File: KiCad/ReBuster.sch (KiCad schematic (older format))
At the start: 11 parts, among them U3 SN74CBTD16210, U4 SN74LVC16T245DGVR, U5 SN74CBTD16210, U6 SN74CBTD16210, U7 74LVC2T45DC, U8 PLCC_84_plug, U9 PLCC_84_plug

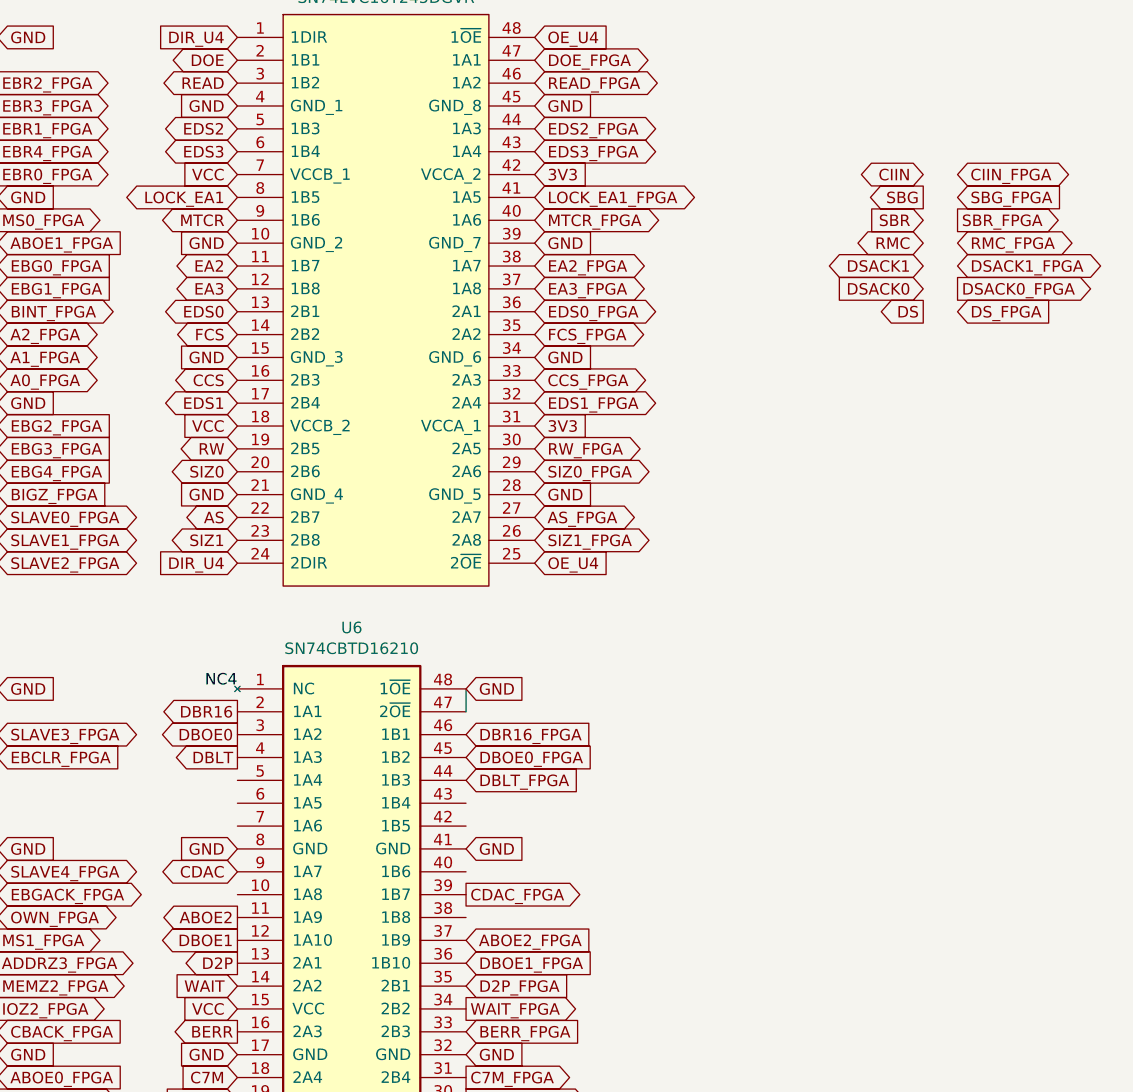
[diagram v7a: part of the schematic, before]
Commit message: Route RMC, SBR, SBG, CIIN to U6 (SN74CBTD16210) and assign pins K10, K11, K12, H13 in FPGA respectively
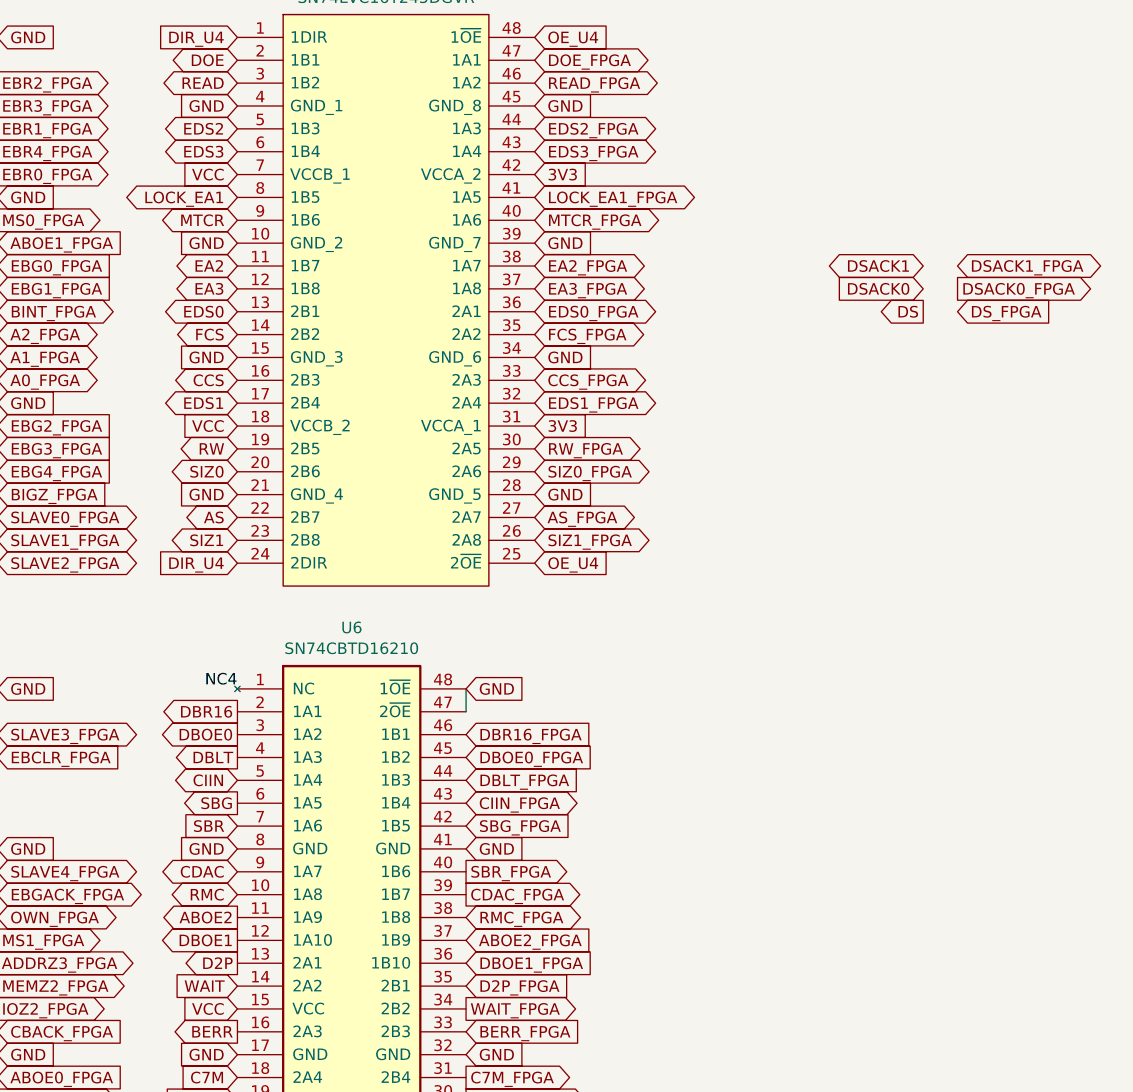
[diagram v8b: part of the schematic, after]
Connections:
- net CIIN: now also U6.5 (1A4)
- net CIIN_FPGA: now also U6.43 (1B4)
- net RMC: now also U6.10 (1A8)
- net RMC_FPGA: now also U6.38 (1B8)
- net SBG: now also U6.6 (1A5)
- net SBG_FPGA: now also U6.42 (1B5)
- net SBR: now also U6.7 (1A6)
- net SBR_FPGA: now also U6.40 (1B6)
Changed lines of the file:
@@
 Text GLabel 5650 6950 0    50   BiDi ~ 0
 MTACK_FPGA
-Text GLabel 12350 1550 2    50   BiDi ~ 0
+Text GLabel 10200 4300 2    50   BiDi ~ 0
 CIIN_FPGA
-Text GLabel 12350 1750 2    50   Output ~ 0
+Text GLabel 10200 4600 2    50   Output ~ 0
 SBR_FPGA
-Text GLabel 12350 1850 2    50   BiDi ~ 0
+Text GLabel 10200 4800 2    50   BiDi ~ 0
 RMC_FPGA
 Text GLabel 10500 2450 2    50   BiDi ~ 0
@@
 Text GLabel 8150 2350 2    50   BiDi ~ 0
 A1_FPGA
-Text GLabel 12350 1650 2    50   Input ~ 0
+Text GLabel 10200 4400 2    50   Input ~ 0
 SBG_FPGA
 Text GLabel 10500 2750 2    50   BiDi ~ 0
@@
 Wire Wire Line
 	2750 5900 2750 6000
-Text GLabel 12200 1850 0    50   BiDi ~ 0
+Text GLabel 9200 4700 0    50   BiDi ~ 0
 RMC
-Text GLabel 12200 1750 0    50   Input ~ 0
+Text GLabel 9200 4400 0    50   Input ~ 0
 SBR
-Text GLabel 12200 1650 0    50   Output ~ 0
+Text GLabel 9200 4300 0    50   Output ~ 0
 SBG
-Text GLabel 12200 1550 0    50   BiDi ~ 0
+Text GLabel 9200 4200 0    50   BiDi ~ 0
 CIIN
 Wire Wire Line
